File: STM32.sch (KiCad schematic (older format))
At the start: 20 parts, among them U2 STM32F303CBTx

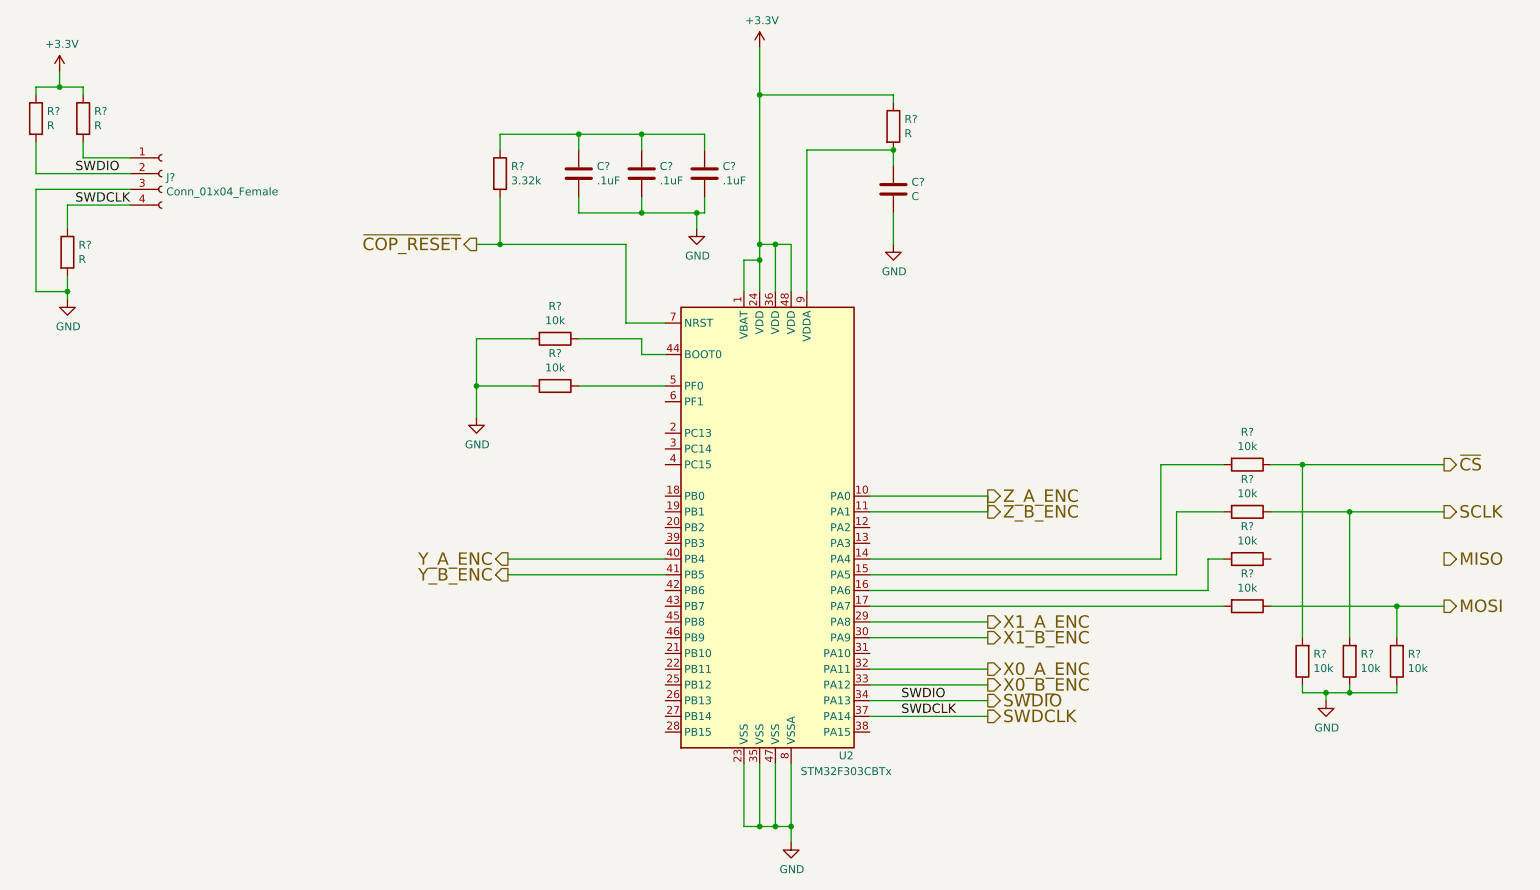
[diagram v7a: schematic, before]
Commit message: cleaned encoder rx. removed PU from CoP rst. misc other CoP updates
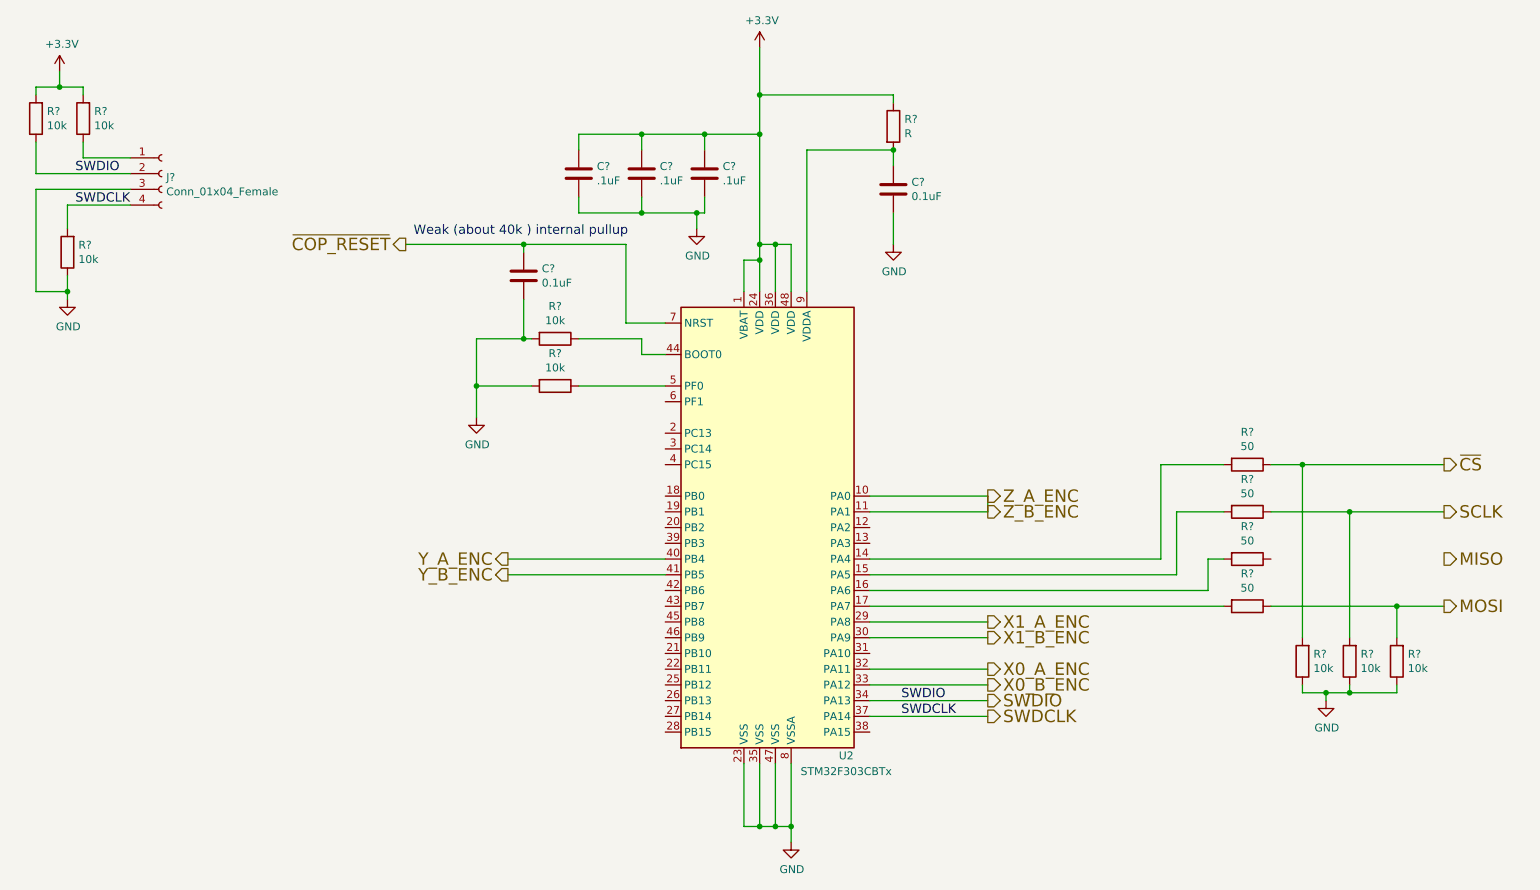
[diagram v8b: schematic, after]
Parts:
- removed R?: 3.32k, Resistor_SMD:R_0805_2012Metric_Pad1.15x1.40mm_HandSolder, symbol Device:R
- removed R? (x3): 10k, Resistor_SMD:R_0805_2012Metric_Pad1.15x1.40mm_HandSolder, symbol Device:R
- removed R? (x3): R, symbol Device:R
- added C?: 0.1uF, Capacitor_SMD:C_0603_1608Metric_Pad1.05x0.95mm_HandSolder, symbol Device:C
- added R? (x3): 50, Resistor_SMD:R_0805_2012Metric_Pad1.15x1.40mm_HandSolder, symbol Device:R
- added R? (x3): 10k, Resistor_SMD:R_0805_2012Metric_Pad1.15x1.40mm_HandSolder, symbol Device:R
- C?: value C -> 0.1uF; footprint (none) -> Capacitor_SMD:C_0603_1608Metric_Pad1.05x0.95mm_HandSolder
- R?: value 10k -> 50
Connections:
- net +3V3: now also C?.1, C?.1, C?.1, R?.2, R?.2
- net GND: now also C?.2, R?.1
- net MOSI: now also R?.1
- net SCLK: now also R?.1
- net SWDCLK: now also R?.2
- net SWDIO: now also R?.1
- net ~COP_RESET: now also C?.1
- net at U2.15 (PA5): now also R?.2
- net at U2.16 (PA6): now also R?.2
- net at U2.17 (PA7): now also R?.2
- net at J?.1 (Pin_1): now also R?.1
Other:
- note added: "Weak (about 40k ) internal pullup"
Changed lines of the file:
@@
 AR Path="/5EE7212D/6227D077" Ref="C?"  Part="1"
 F 0 "C?" H 6615 1646 50  0000 L CNN
-F 1 "C" H 6615 1555 50  0000 L CNN
-F 2 "" H 6538 1450 50  0001 C CNN
+F 1 "0.1uF" H 6615 1555 50  0000 L CNN
+F 2 "Capacitor_SMD:C_0603_1608Metric_Pad1.05x0.95mm_HandSolder" H 6538 1450 50  0001 C CNN
 F 3 "~" H 6500 1600 50  0001 C CNN
 	1    6500 1600
@@
 	3850 2850 3850 3050
 Wire Wire Line
-	4200 2550 3850 2550
+	4200 2550 4150 2550
 Wire Wire Line
 	3850 2550 3850 2850
@@
 Wire Wire Line
 	4900 2550 4500 2550
-Text HLabel 3850 1950 0    79   Output ~ 0
+Text HLabel 3400 1950 0    79   Output ~ 0
 ~COP_RESET
 Wire Wire Line
@@
 	4800 2450 4800 1950
 Wire Wire Line
-	4800 1950 4000 1950
-$Comp
-L Device:R R?
-U 1 1 62ABEB6C
-P 4000 1500
-F 0 "R?" H 4070 1546 50  0000 L CNN
-F 1 "3.32k" H 4070 1455 50  0000 L CNN
-F 2 "Resistor_SMD:R_0805_2012Metric_Pad1.15x1.40mm_HandSolder" V 3930 1500 50  0001 C CNN
-F 3 "~" H 4000 1500 50  0001 C CNN
-	1    4000 1500
-	1    0    0    -1
-$EndComp
-Wire Wire Line
-	4000 1350 4000 1250
-Wire Wire Line
-	4000 1250 4500 1250
-Connection ~ 4500 1250
-Wire Wire Line
-	4000 1650 4000 1950
-Connection ~ 4000 1950
-Wire Wire Line
-	4000 1950 3850 1950
+	4800 1950 4150 1950
 $Comp
 L Device:R R?
@@
 $Comp
 L Device:R R?
-U 1 1 62ACD551
-P 8750 4250
-F 0 "R?" V 8543 4250 50  0000 C CNN
-F 1 "10k" V 8634 4250 50  0000 C CNN
-F 2 "Resistor_SMD:R_0805_2012Metric_Pad1.15x1.40mm_HandSolder" V 8680 4250 50  0001 C CNN
-F 3 "~" H 8750 4250 50  0001 C CNN
-	1    8750 4250
-	0    1    1    0
-$EndComp
-$Comp
-L Device:R R?
-U 1 1 62AD0F3F
-P 8750 3950
-F 0 "R?" V 8543 3950 50  0000 C CNN
-F 1 "10k" V 8634 3950 50  0000 C CNN
-F 2 "Resistor_SMD:R_0805_2012Metric_Pad1.15x1.40mm_HandSolder" V 8680 3950 50  0001 C CNN
-F 3 "~" H 8750 3950 50  0001 C CNN
-	1    8750 3950
-	0    1    1    0
-$EndComp
-$Comp
-L Device:R R?
-U 1 1 62AD13DD
-P 8750 3650
-F 0 "R?" V 8543 3650 50  0000 C CNN
-F 1 "10k" V 8634 3650 50  0000 C CNN
-F 2 "Resistor_SMD:R_0805_2012Metric_Pad1.15x1.40mm_HandSolder" V 8680 3650 50  0001 C CNN
-F 3 "~" H 8750 3650 50  0001 C CNN
-	1    8750 3650
-	0    1    1    0
-$EndComp
-$Comp
-L Device:R R?
 U 1 1 62AD17E8
 P 8750 3350
 F 0 "R?" V 8543 3350 50  0000 C CNN
-F 1 "10k" V 8634 3350 50  0000 C CNN
+F 1 "50" V 8634 3350 50  0000 C CNN
 F 2 "Resistor_SMD:R_0805_2012Metric_Pad1.15x1.40mm_HandSolder" V 8680 3350 50  0001 C CNN
 F 3 "~" H 8750 3350 50  0001 C CNN
@@
 	1    0    0    -1
 $EndComp
-Wire Wire Line
-	5650 1000 5650 1950
 $Comp
 L Device:C C?
@@
 	1    0    0    -1
 $EndComp
-$Comp
-L Device:R R?
-U 1 1 62B05695
-P 1250 2000
-F 0 "R?" H 1320 2046 50  0000 L CNN
-F 1 "R" H 1320 1955 50  0000 L CNN
-F 2 "" V 1180 2000 50  0001 C CNN
-F 3 "~" H 1250 2000 50  0001 C CNN
-	1    1250 2000
-	1    0    0    -1
-$EndComp
-$Comp
-L Device:R R?
-U 1 1 62B058F3
-P 1050 1150
-F 0 "R?" H 1120 1196 50  0000 L CNN
-F 1 "R" H 1120 1105 50  0000 L CNN
-F 2 "" V 980 1150 50  0001 C CNN
-F 3 "~" H 1050 1150 50  0001 C CNN
-	1    1050 1150
-	1    0    0    -1
-$EndComp
-$Comp
-L Device:R R?
-U 1 1 62B08BC2
-P 1350 1150
-F 0 "R?" H 1420 1196 50  0000 L CNN
-F 1 "R" H 1420 1105 50  0000 L CNN
-F 2 "" V 1280 1150 50  0001 C CNN
-F 3 "~" H 1350 1150 50  0001 C CNN
-	1    1350 1150
-	1    0    0    -1
-$EndComp
 Wire Wire Line
 	1650 1400 1350 1400
@@
 Text Label 1300 1700 0    59   ~ 0
 SWDCLK
+$Comp
+L Device:R R?
+U 1 1 62B3A1E5
+P 8750 3650
+F 0 "R?" V 8543 3650 50  0000 C CNN
+F 1 "50" V 8634 3650 50  0000 C CNN
+F 2 "Resistor_SMD:R_0805_2012Metric_Pad1.15x1.40mm_HandSolder" V 8680 3650 50  0001 C CNN
+F 3 "~" H 8750 3650 50  0001 C CNN
+	1    8750 3650
+	0    1    1    0
+$EndComp
+$Comp
+L Device:R R?
+U 1 1 62B3A476
+P 8750 3950
+F 0 "R?" V 8543 3950 50  0000 C CNN
+F 1 "50" V 8634 3950 50  0000 C CNN
+F 2 "Resistor_SMD:R_0805_2012Metric_Pad1.15x1.40mm_HandSolder" V 8680 3950 50  0001 C CNN
+F 3 "~" H 8750 3950 50  0001 C CNN
+	1    8750 3950
+	0    1    1    0
+$EndComp
+$Comp
+L Device:R R?
+U 1 1 62B3A881
+P 8750 4250
+F 0 "R?" V 8543 4250 50  0000 C CNN
+F 1 "50" V 8634 4250 50  0000 C CNN
+F 2 "Resistor_SMD:R_0805_2012Metric_Pad1.15x1.40mm_HandSolder" V 8680 4250 50  0001 C CNN
+F 3 "~" H 8750 4250 50  0001 C CNN
+	1    8750 4250
+	0    1    1    0
+$EndComp
+$Comp
+L Device:R R?
+U 1 1 62B3AE73
+P 1350 1150
+F 0 "R?" H 1280 1104 50  0000 R CNN
+F 1 "10k" H 1280 1195 50  0000 R CNN
+F 2 "Resistor_SMD:R_0805_2012Metric_Pad1.15x1.40mm_HandSolder" V 1280 1150 50  0001 C CNN
+F 3 "~" H 1350 1150 50  0001 C CNN
+	1    1350 1150
+	-1   0    0    1
+$EndComp
+$Comp
+L Device:R R?
+U 1 1 62B3B3A7
+P 1250 2000
+F 0 "R?" H 1180 1954 50  0000 R CNN
+F 1 "10k" H 1180 2045 50  0000 R CNN
+F 2 "Resistor_SMD:R_0805_2012Metric_Pad1.15x1.40mm_HandSolder" V 1180 2000 50  0001 C CNN
+F 3 "~" H 1250 2000 50  0001 C CNN
+	1    1250 2000
+	-1   0    0    1
+$EndComp
+$Comp
+L Device:R R?
+U 1 1 62B3BA13
+P 1050 1150
+F 0 "R?" H 980 1104 50  0000 R CNN
+F 1 "10k" H 980 1195 50  0000 R CNN
+F 2 "Resistor_SMD:R_0805_2012Metric_Pad1.15x1.40mm_HandSolder" V 980 1150 50  0001 C CNN
+F 3 "~" H 1050 1150 50  0001 C CNN
+	1    1050 1150
+	-1   0    0    1
+$EndComp
+$Comp
+L Device:C C?
+U 1 1 62B3D441
+P 4150 2150
+AR Path="/5EE66603/62B3D441" Ref="C?"  Part="1"
+AR Path="/5EE7212D/62B3D441" Ref="C?"  Part="1"
+F 0 "C?" H 4265 2196 50  0000 L CNN
+F 1 "0.1uF" H 4265 2105 50  0000 L CNN
+F 2 "Capacitor_SMD:C_0603_1608Metric_Pad1.05x0.95mm_HandSolder" H 4188 2000 50  0001 C CNN
+F 3 "~" H 4150 2150 50  0001 C CNN
+	1    4150 2150
+	1    0    0    -1
+$EndComp
+Wire Wire Line
+	4150 2300 4150 2550
+Connection ~ 4150 2550
+Wire Wire Line
+	4150 2550 3850 2550
+Wire Wire Line
+	4150 2000 4150 1950
+Connection ~ 4150 1950
+Wire Wire Line
+	5650 1000 5650 1250
+Wire Wire Line
+	5300 1250 5650 1250
+Connection ~ 5300 1250
+Connection ~ 5650 1250
+Wire Wire Line
+	5650 1250 5650 1950
+Wire Wire Line
+	3400 1950 4150 1950
+Text Notes 3450 1900 0    59   ~ 0
+Weak (about 40k ) internal pullup
 $EndSCHEMATC
